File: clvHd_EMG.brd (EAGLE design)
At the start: 21 x 18.5 mm, 25 parts, among them J1 XF2J-1824-12, J2 XF2J-1824-12, U1 ADS1293CISQ/NOPB

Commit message: shrinken
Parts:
- removed J1, J2: XF2J-1824-12, con-omron:XF2J-1824-12
- added 1, 2: X05C2018TZ, con-omron:X05C2018TZ
- moved R7 1.60 mm to (19.4, 11.4)
- moved L1 1.53 mm to (18.9, 13.0)
- moved R13 1.40 mm to (15.0, 4.95)
- moved R10 1.14 mm to (13.2, 4.45)
- moved U$1 1.00 mm to (17.5, 4.64)
- moved C10 0.98 mm to (18.4, 1.90)
- moved C12 0.90 mm to (9.45, 8.70)
- moved C16 0.90 mm to (17.2, 11.0)
- moved C19 0.90 mm to (18.3, 11.0)
- moved C20 0.90 mm to (18.8, 8.45)
- moved C9 0.90 mm to (18.4, 7.35)
- moved L3 0.90 mm to (6.20, 9.10)
- moved R1 0.90 mm to (6.10, 11.3)
- moved R12 0.90 mm to (6.75, 7.40)
- moved R15 0.90 mm to (8.90, 11.0)
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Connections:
- net A0: now also 1.3; no longer J1.16
- net A1: now also 1.5; no longer J1.14
- net A2: now also 1.6; no longer J1.13
- net A3: now also 1.8; no longer J1.11
- net CLK: now also 1.16, 2.3; no longer J1.3, J2.16
- net DIN: now also 1.13, 2.6; no longer J1.6, J2.13
- net DOUT: now also 1.15, 2.4; no longer J1.4, J2.15
- net GND: now also 1.11, 1.14, 1.17, 1.4, 1.7, 2.12, 2.15, 2.2, 2.5, 2.8; no longer J1.12, J1.15, J1.2, J1.5, J1.8, J2.11, J2.14, J2.17, J2.4, J2.7
- net GPIO1: now also 1.2, 2.17; no longer J1.17, J2.2
- net IN5: now also 1.1, 2.18; no longer J1.18, J2.1
- net RST: now also 1.9, 2.10; no longer J1.10, J2.9
- net S0: now also 2.16; no longer J2.3
- net S1: now also 2.14; no longer J2.5
- net S2: now also 2.13; no longer J2.6
- net S3: now also 2.11; no longer J2.8
- net SCLK: now also 1.12, 2.7; no longer J1.7, J2.12
- net SYNCB: now also 1.10, 2.9; no longer J1.9, J2.10
- net VDD: now also 1.18, 2.1; no longer J1.1, J2.18
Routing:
- net GND: track 54.7 -> 52.1 mm
- net A2: track 30.4 -> 27.8 mm
- net DOUT: track 19.6 -> 18.0 mm
- net N$16: track 21.5 -> 19.9 mm
- net S2: track 24.9 -> 23.5 mm
- net DIN: track 22.6 -> 21.3 mm
- net CLK: track 21.7 -> 20.5 mm
- net VDD: track 69.2 -> 68.0 mm
- net IN6: track 12.1 -> 10.9 mm
- net IN5: track 25.4 -> 24.3 mm
- net GPIO1: track 25.1 -> 24.1 mm
- net SYNCB: track 23.7 -> 22.8 mm
- net SCLK: track 21.4 -> 20.4 mm
- net A0: track 12.8 -> 12.2 mm
- net S3: track 17.0 -> 16.4 mm
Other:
- board size 21 x 18.5 mm -> 21 x 17 mm
- board text added: "ads1293-v2.2"
- board text removed: "ads1293-v2.1"

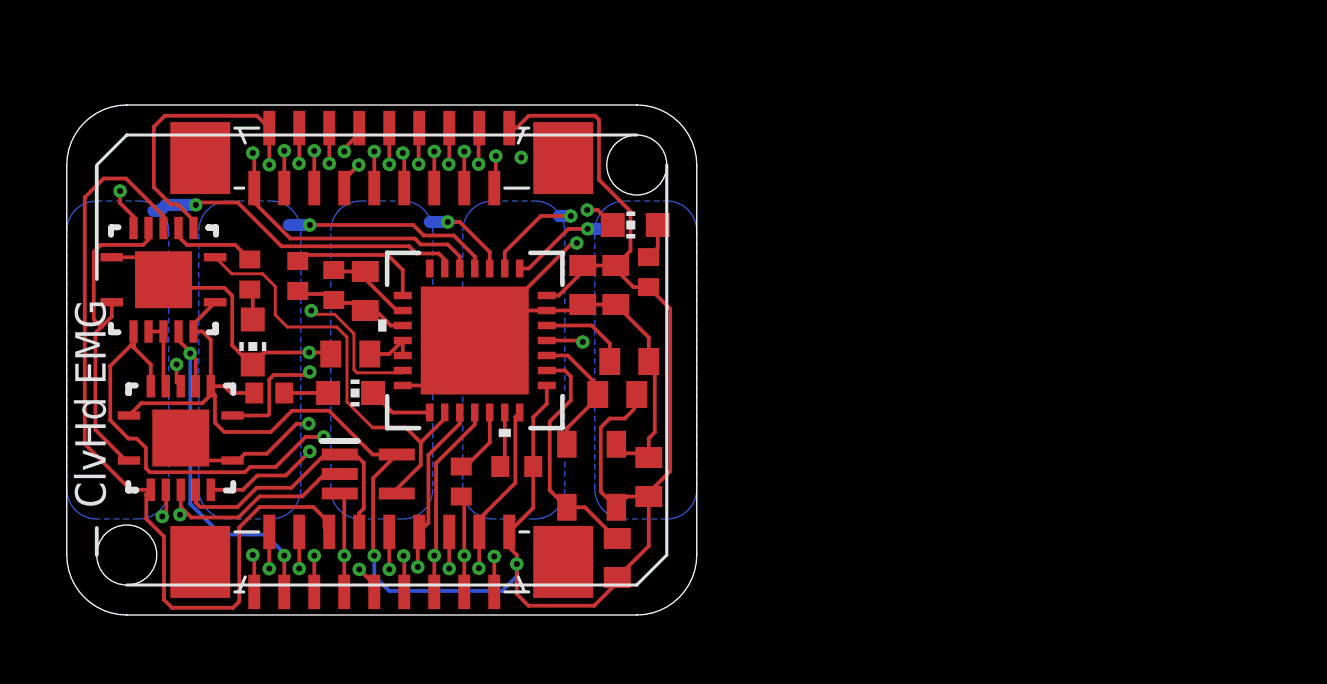
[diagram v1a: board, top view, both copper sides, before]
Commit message: dir indication + lvl3 gnd plane
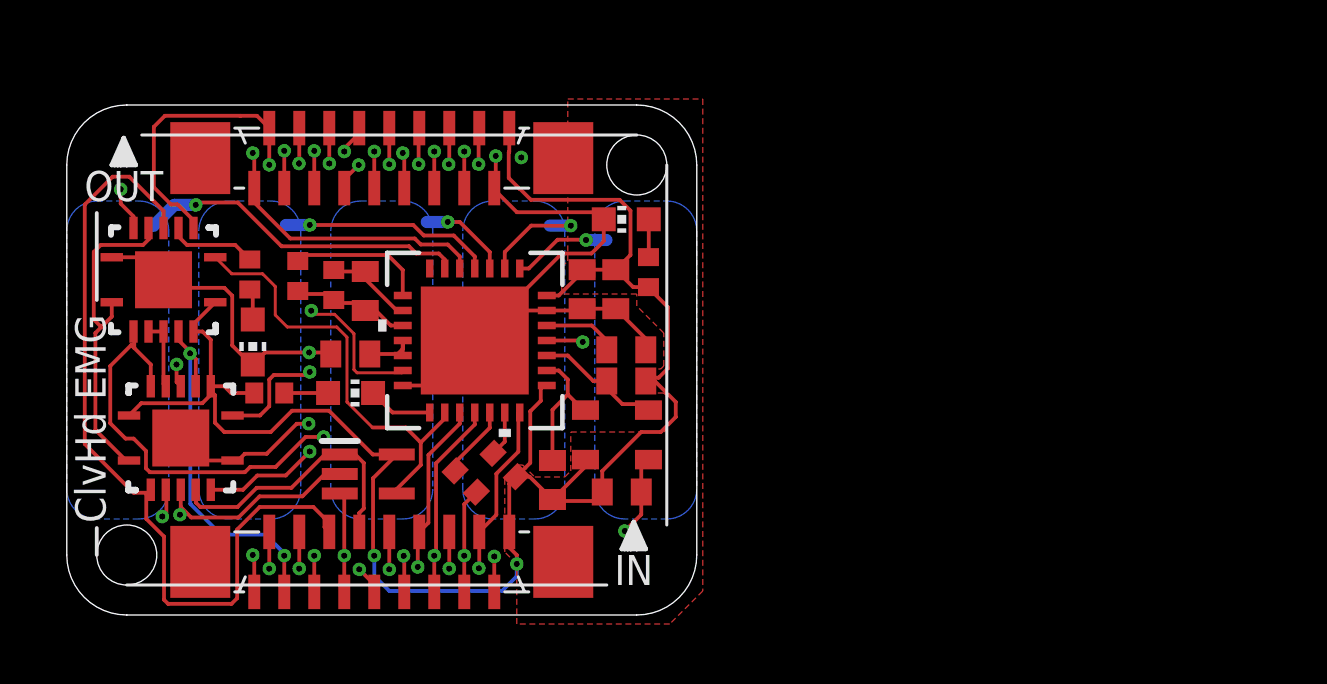
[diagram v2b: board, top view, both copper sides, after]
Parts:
- moved C10 3.38 mm to (16.2, 4.50)
- moved U$1 1.61 mm to (18.3, 6.00), turned to 0 degrees
- moved C13 1.03 mm to (18.5, 4.10), turned to 0 degrees
- moved C9 0.54 mm to (18.6, 7.80)
- moved R13 0.40 mm to (14.6, 5.00), turned to 315 degrees
- moved C20 0.40 mm to (18.6, 8.84)
- moved L1 0.36 mm to (18.6, 13.2)
- moved R10 0.15 mm to (13.3, 4.45), turned to 315 degrees
- moved C16 0.14 mm to (17.2, 10.9)
- moved C19 0.14 mm to (18.3, 10.9)
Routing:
- net VDD: track 68.0 -> 60.4 mm
- net N$4: track 7.88 -> 4.54 mm
- net GND: track 52.1 -> 53.7 mm, vias 14 -> 13
- added copper zone on layer 15, net GND
- added copper zone on layer 1, net VDD
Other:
- board text added: "IN"
- board text added: "OUT"

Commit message: double gate nand
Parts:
- AND_IC: value SN74ALVC08LARGE -> SN74ALVC08RGY-LARGE; device SamacSys_Parts:SN74LVC86ARGYR -> SamacSys_Parts:VQFN-14-CUSTOM
- L1: value LED 0603 -> Green
- L2: value LED 0603 -> Red
- L3: value LED 0603 -> White
- NAND_IC: value SN74LVC1G132DCKT -> SN74AUP2G00YZP; device SamacSys_Parts:SOT65P210X110-5N -> SamacSys_Parts:DSBGA
- R1, R12, R7: value 100 -> 51
- XOR_IC: value SN74LVC86A -> SN74LVC86ARGY-LARGE; device SamacSys_Parts:SN74LVC86ARGYR -> SamacSys_Parts:VQFN-14-CUSTOM
- moved NAND_IC 0.50 mm to (10.1, 5.20), turned to 90 degrees
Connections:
- new net N$1: AND_IC.1, NAND_IC.B2
- net A3: now also NAND_IC.A1; no longer NAND_IC.1
- net CS: now also NAND_IC.C1, NAND_IC.C2; no longer AND_IC.1, NAND_IC.4
- net GND: now also NAND_IC.D1; no longer NAND_IC.3
- net N$16: now also NAND_IC.B1; no longer NAND_IC.2
- net VDD: now also NAND_IC.A2, NAND_IC.D2; no longer NAND_IC.5
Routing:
- net CS: track 14.6 -> 3.43 mm
- net N$1: track 0.00 -> 9.70 mm
- net VDD: track 60.4 -> 64.7 mm, vias 2 -> 3
- net A3: track 9.29 -> 10.8 mm, vias 0 -> 2
- net DIN: track 21.2 -> 19.9 mm, vias 2 -> 3
- net RST: track 31.7 -> 30.5 mm
- net N$16: track 20.0 -> 21.0 mm
- net GND: track 53.7 -> 54.6 mm
- net SYNCB: track 22.8 -> 22.2 mm
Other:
- board text added: "ads1293-v2.3"
- board text removed: "ads1293-v2.2"

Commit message: long board
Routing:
- net IN1: track 3.29 -> 22.5 mm, vias 1 -> 2
- net IN2: track 3.81 -> 16.2 mm, vias 1 -> 2
- net IN3: track 3.06 -> 10.2 mm
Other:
- board size 21 x 17 mm -> 40 x 17 mm
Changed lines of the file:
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@@
 <setting verticaltext="up"/>
 </settings>
-<grid distance="0.01" unitdist="mm" unit="mm" style="lines" multiple="1" display="yes" altdistance="0.1" altunitdist="mm" altunit="mm"/>
+<grid distance="1" unitdist="mm" unit="mm" style="lines" multiple="1" display="yes" altdistance="0.1" altunitdist="mm" altunit="mm"/>
 <layers>
 <layer number="1" name="Top" color="4" fill="1" visible="yes" active="yes"/>
@@
 <layer number="43" name="vRestrict" color="2" fill="10" visible="no" active="yes"/>
 <layer number="44" name="Drills" color="7" fill="1" visible="no" active="yes"/>
-<layer number="45" name="Holes" color="7" fill="1" visible="no" active="yes"/>
+<layer number="45" name="Holes" color="7" fill="1" visible="yes" active="yes"/>
 <layer number="46" name="Milling" color="3" fill="1" visible="no" active="yes"/>
 <layer number="47" name="Measures" color="7" fill="1" visible="no" active="yes"/>
@@
 <text x="18" y="1.2" size="1" layer="26" rot="MR0" align="center-left">Designed by Aightech</text>
 <wire x1="0" y1="15" x2="0" y2="2" width="0" layer="20"/>
-<wire x1="2" y1="0" x2="19" y2="0" width="0" layer="20"/>
-<wire x1="21" y1="2" x2="21" y2="15" width="0" layer="20"/>
-<wire x1="19" y1="17" x2="2" y2="17" width="0" layer="20"/>
+<wire x1="2" y1="0" x2="38" y2="0" width="0" layer="20"/>
+<wire x1="40" y1="2" x2="40" y2="15" width="0" layer="20"/>
+<wire x1="38" y1="17" x2="2" y2="17" width="0" layer="20"/>
 <text x="1.7" y="14.5" size="1" layer="26" rot="MR0" align="center">5</text>
 <text x="19.3" y="2.3" size="1" layer="26" rot="MR0" align="center">1</text>
@@
 </polygon>
 <polygon width="0.01" layer="30">
-<vertex x="8.9" y="4.3"/>
-<vertex x="8.9" y="12.7" curve="-90"/>
-<vertex x="9.9" y="13.7"/>
-<vertex x="11.1" y="13.7" curve="-90"/>
-<vertex x="12.1" y="12.7"/>
-<vertex x="12.1" y="4.3" curve="-90"/>
-<vertex x="11.1" y="3.3"/>
-<vertex x="9.9" y="3.3" curve="-90"/>
+<vertex x="18.9" y="4.3"/>
+<vertex x="18.9" y="12.7" curve="-90"/>
+<vertex x="19.9" y="13.7"/>
+<vertex x="21.1" y="13.7" curve="-90"/>
+<vertex x="22.1" y="12.7"/>
+<vertex x="22.1" y="4.3" curve="-90"/>
+<vertex x="21.1" y="3.3"/>
+<vertex x="19.9" y="3.3" curve="-90"/>
 </polygon>
 <polygon width="0.01" layer="30">
-<vertex x="13.3" y="4.3"/>
-<vertex x="13.3" y="12.7" curve="-90"/>
-<vertex x="14.3" y="13.7"/>
-<vertex x="15.5" y="13.7" curve="-90"/>
-<vertex x="16.5" y="12.7"/>
-<vertex x="16.5" y="4.3" curve="-90"/>
-<vertex x="15.5" y="3.3"/>
-<vertex x="14.3" y="3.3" curve="-90"/>
+<vertex x="29.3" y="4.3"/>
+<vertex x="29.3" y="12.7" curve="-90"/>
+<vertex x="30.3" y="13.7"/>
+<vertex x="31.5" y="13.7" curve="-90"/>
+<vertex x="32.5" y="12.7"/>
+<vertex x="32.5" y="4.3" curve="-90"/>
+<vertex x="31.5" y="3.3"/>
+<vertex x="30.3" y="3.3" curve="-90"/>
 </polygon>
 <polygon width="0.01" layer="30">
-<vertex x="17.7" y="4.3"/>
-<vertex x="17.7" y="12.7" curve="-90"/>
-<vertex x="18.7" y="13.7"/>
-<vertex x="19.8" y="13.7" curve="-90"/>
-<vertex x="20.8" y="12.7"/>
-<vertex x="20.8" y="4.3" curve="-90"/>
-<vertex x="19.8" y="3.3"/>
-<vertex x="18.7" y="3.3" curve="-90"/>
+<vertex x="36.7" y="4.3"/>
+<vertex x="36.7" y="12.7" curve="-90"/>
+<vertex x="37.7" y="13.7"/>
+<vertex x="38.8" y="13.7" curve="-90"/>
+<vertex x="39.8" y="12.7"/>
+<vertex x="39.8" y="4.3" curve="-90"/>
+<vertex x="38.8" y="3.3"/>
+<vertex x="37.7" y="3.3" curve="-90"/>
 </polygon>
 <wire x1="2" y1="0" x2="0" y2="2" width="0" layer="20" curve="-90"/>
 <wire x1="0" y1="15" x2="2" y2="17" width="0" layer="20" curve="-90"/>
-<wire x1="19" y1="17" x2="21" y2="15" width="0" layer="20" curve="-90"/>
-<wire x1="21" y1="2" x2="19" y2="0" width="0" layer="20" curve="-90"/>
-<hole x="2" y="2" drill="2"/>
-<hole x="19" y="15" drill="2"/>
+<wire x1="38" y1="17" x2="40" y2="15" width="0" layer="20" curve="-90"/>
+<wire x1="40" y1="2" x2="38" y2="0" width="0" layer="20" curve="-90"/>
+<hole x="2" y="2" drill="1.6"/>
+<hole x="38" y="15" drill="1.6"/>
 <wire x1="2" y1="1" x2="18" y2="1" width="0.1016" layer="25"/>
 <wire x1="20" y1="3" x2="20" y2="15" width="0.1016" layer="25"/>
@@
 <wire x1="13.24" y1="15.44" x2="13.24" y2="14.78" width="0.127" layer="15"/>
 <wire x1="13.37531875" y1="14.64468125" x2="13.24" y2="14.78" width="0.127" layer="15"/>
-<wire x1="13.27866875" y1="2.13866875" x2="13.25" y2="2.11" width="0.127" layer="15"/>
-<wire x1="13.25" y1="2.11" x2="13.25" y2="1.98" width="0.127" layer="15"/>
 <via x="13.25" y="1.98" extent="1-16" drill="0.2"/>
 <contactref element="2" pad="4"/>
@@
 <via x="12.7" y="13.1" extent="1-16" drill="0.2"/>
 <polygon width="0.01" layer="16">
-<vertex x="8.8" y="4.2"/>
-<vertex x="8.8" y="12.8" curve="-90"/>
-<vertex x="9.8" y="13.8"/>
-<vertex x="11.2" y="13.8" curve="-90"/>
-<vertex x="12.2" y="12.8"/>
-<vertex x="12.2" y="4.2" curve="-90"/>
-<vertex x="11.2" y="3.2"/>
-<vertex x="9.8" y="3.2" curve="-90"/>
+<vertex x="18.8" y="4.2"/>
+<vertex x="18.8" y="12.8" curve="-90"/>
+<vertex x="19.8" y="13.8"/>
+<vertex x="21.2" y="13.8" curve="-90"/>
+<vertex x="22.2" y="12.8"/>
+<vertex x="22.2" y="4.2" curve="-90"/>
+<vertex x="21.2" y="3.2"/>
+<vertex x="19.8" y="3.2" curve="-90"/>
 </polygon>
-<wire x1="12.7" y1="13.1" x2="12" y2="13.1" width="0.4064" layer="16"/>
+<wire x1="20.26" y1="13.54" x2="12.98" y2="13.54" width="0.4064" layer="16"/>
+<wire x1="12.7" y1="13.1" x2="12.7" y2="13.26" width="0.4064" layer="16"/>
+<wire x1="12.98" y1="13.54" x2="12.7" y2="13.26" width="0.4064" layer="16"/>
 </signal>
 <signal name="IN5">
@@
 <via x="17.31" y="12.5" extent="1-16" drill="0.2"/>
 <polygon width="0.01" layer="16">
-<vertex x="17.6" y="4.2"/>
-<vertex x="17.6" y="12.8" curve="-90"/>
-<vertex x="18.6" y="13.8"/>
-<vertex x="20" y="13.8" curve="-90"/>
-<vertex x="21" y="12.8"/>
-<vertex x="21" y="4.2" curve="-90"/>
-<vertex x="20" y="3.2"/>
-<vertex x="18.6" y="3.2" curve="-90"/>
+<vertex x="36.6" y="4.2"/>
+<vertex x="36.6" y="12.8" curve="-90"/>
+<vertex x="37.6" y="13.8"/>
+<vertex x="39" y="13.8" curve="-90"/>
+<vertex x="40" y="12.8"/>
+<vertex x="40" y="4.2" curve="-90"/>
+<vertex x="39" y="3.2"/>
+<vertex x="37.6" y="3.2" curve="-90"/>
 </polygon>
-<wire x1="17.31" y1="12.5" x2="17.99" y2="12.5" width="0.4064" layer="16"/>
+<wire x1="17.57" y1="12.24" x2="35.92" y2="12.24" width="0.4064" layer="15"/>
+<wire x1="17.57" y1="12.24" x2="17.31" y2="12.5" width="0.4064" layer="15"/>
+<via x="35.92" y="12.24" extent="1-16" drill="0.35"/>
+<wire x1="35.92" y1="12.24" x2="37.06" y2="12.24" width="0.6096" layer="16"/>
+<wire x1="37.06" y1="12.24" x2="37.1" y2="12.2" width="0.6096" layer="16"/>
 </signal>
 <signal name="VDD">
@@
 <polygon width="0.1524" layer="2">
 <vertex x="0" y="17"/>
-<vertex x="21" y="17"/>
-<vertex x="21" y="0"/>
+<vertex x="40" y="17"/>
+<vertex x="40" y="0"/>
 <vertex x="0" y="0"/>
 </polygon>
@@
 <signal name="IN2">
 <polygon width="0.01" layer="16">
-<vertex x="13.2" y="4.2"/>
-<vertex x="13.2" y="12.8" curve="-90"/>
-<vertex x="14.2" y="13.8"/>
-<vertex x="15.6" y="13.8" curve="-90"/>
-<vertex x="16.6" y="12.8"/>
-<vertex x="16.6" y="4.2" curve="-90"/>
-<vertex x="15.6" y="3.2"/>
-<vertex x="14.2" y="3.2" curve="-90"/>
+<vertex x="29.2" y="4.2"/>
+<vertex x="29.2" y="12.8" curve="-90"/>
+<vertex x="30.2" y="13.8"/>
+<vertex x="31.6" y="13.8" curve="-90"/>
+<vertex x="32.6" y="12.8"/>
+<vertex x="32.6" y="4.2" curve="-90"/>
+<vertex x="31.6" y="3.2"/>
+<vertex x="30.2" y="3.2" curve="-90"/>
 </polygon>
 <contactref element="U1" pad="2"/>
@@
 <wire x1="14.6" y1="12.1" x2="14.6" y2="11.55" width="0.127" layer="1"/>
 <via x="16.8" y="12.98" extent="1-16" drill="0.2"/>
-<wire x1="16.8" y1="12.98" x2="16.1" y2="12.98" width="0.4064" layer="16"/>
+<wire x1="16.8" y1="12.98" x2="16.8" y2="13.08" width="0.4064" layer="15"/>
+<wire x1="17.11" y1="13.39" x2="16.8" y2="13.08" width="0.4064" layer="15"/>
+<wire x1="17.11" y1="13.39" x2="28.72" y2="13.39" width="0.4064" layer="15"/>
+<via x="28.72" y="13.39" extent="1-16" drill="0.35"/>
+<wire x1="28.72" y1="13.39" x2="29.51" y2="13.39" width="0.6096" layer="16"/>
+<wire x1="29.51" y1="13.39" x2="29.6" y2="13.3" width="0.6096" layer="16"/>
 </signal>
 <signal name="A1">
@@
 <wire x1="3.225" y1="13.47" x2="3.225" y2="12.9" width="0.127" layer="1"/>
 <contactref element="1" pad="6"/>
-<wire x1="2.73" y1="3.12546875" x2="3.2413" y2="2.61416875" width="0.127" layer="1"/>
-<wire x1="3.2413" y1="2.61416875" x2="3.2413" y2="0.5087" width="0.127" layer="1"/>
-<wire x1="2.73" y1="4.105" x2="2.73" y2="3.12546875" width="0.127" layer="1"/>
-<wire x1="3.2413" y1="0.5087" x2="3.3787" y2="0.3713" width="0.127" layer="1"/>
+<wire x1="2.73" y1="3.140590625" x2="3.25809375" y2="2.612496875" width="0.127" layer="1"/>
+<wire x1="3.25809375" y1="2.612496875" x2="3.25809375" y2="0.49190625" width="0.127" layer="1"/>
+<wire x1="2.73" y1="4.105" x2="2.73" y2="3.140590625" width="0.127" layer="1"/>
+<wire x1="3.25809375" y1="0.49190625" x2="3.3787" y2="0.3713" width="0.127" layer="1"/>
 <wire x1="8.7505" y1="3.06890625" x2="8.7505" y2="2.7705" width="0.127" layer="1"/>
 <wire x1="8.75" y1="2.77" x2="8.7505" y2="2.7705" width="0.127" layer="1"/>
